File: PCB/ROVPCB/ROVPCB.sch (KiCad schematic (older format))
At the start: 7 parts, among them J1 Conn_01x04_Male, J2 Conn_01x04_Male, P1 Conn_02x20_Odd_Even

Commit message: Added Accelerometer to schematic and Board.
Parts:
- added C1: 10nF, Capacitor_SMD:C_0603_1608Metric, symbol Device:C
- added C2: 0.1uF, Capacitor_SMD:C_0603_1608Metric, symbol Device:C
- added C3: 2.2 nF, Capacitor_SMD:C_0603_1608Metric, symbol Device:C
- added U1: MPU-6050, Sensor_Motion:InvenSense_QFN-24_4x4mm_P0.5mm, symbol Sensor_Motion:MPU-6050
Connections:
- wire segments 63 -> 81
- no-connect marks 0 -> 3
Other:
- note added: "Accelerometer"
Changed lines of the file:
@@
 Wire Wire Line
 	7100 2250 8050 2250
+$Comp
+L Sensor_Motion:MPU-6050 U1
+U 1 1 5C61FB5F
+P 2550 5350
+F 0 "U1" H 2550 4564 50  0000 C CNN
+F 1 "MPU-6050" H 2550 4473 50  0000 C CNN
+F 2 "Sensor_Motion:InvenSense_QFN-24_4x4mm_P0.5mm" H 2550 4550 50  0001 C CNN
+F 3 "https://store.invensense.com/datasheets/invensense/MPU-6050_DataSheet_V3%204.pdf" H 2550 5200 50  0001 C CNN
+	1    2550 5350
+	1    0    0    -1
+$EndComp
+Text Notes 1650 4050 0    157  ~ 31
+Accelerometer
+$Comp
+L ROVPCB-rescue:GND-power #PWR0101
+U 1 1 5C61FCB6
+P 1700 5700
+F 0 "#PWR0101" H 1700 5450 50  0001 C CNN
+F 1 "GND" H 1700 5550 50  0000 C CNN
+F 2 "" H 1700 5700 50  0000 C CNN
+F 3 "" H 1700 5700 50  0000 C CNN
+	1    1700 5700
+	1    0    0    -1
+$EndComp
+Wire Wire Line
+	1850 5550 1700 5550
+Wire Wire Line
+	1700 5550 1700 5650
+Wire Wire Line
+	1850 5650 1800 5650
+Connection ~ 1700 5650
+Wire Wire Line
+	1700 5650 1700 5700
+$Comp
+L Device:C C2
+U 1 1 5C622699
+P 3450 5800
+F 0 "C2" H 3565 5846 50  0000 L CNN
+F 1 "0.1uF" H 3565 5755 50  0000 L CNN
+F 2 "Capacitor_SMD:C_0603_1608Metric" H 3488 5650 50  0001 C CNN
+F 3 "~" H 3450 5800 50  0001 C CNN
+	1    3450 5800
+	1    0    0    -1
+$EndComp
+$Comp
+L Device:C C3
+U 1 1 5C622707
+P 3900 5800
+F 0 "C3" H 4015 5846 50  0000 L CNN
+F 1 "2.2 nF" H 4015 5755 50  0000 L CNN
+F 2 "Capacitor_SMD:C_0603_1608Metric" H 3938 5650 50  0001 C CNN
+F 3 "~" H 3900 5800 50  0001 C CNN
+	1    3900 5800
+	1    0    0    -1
+$EndComp
+Wire Wire Line
+	3250 5650 3450 5650
+$Comp
+L ROVPCB-rescue:GND-power #PWR0102
+U 1 1 5C62556F
+P 3450 5950
+F 0 "#PWR0102" H 3450 5700 50  0001 C CNN
+F 1 "GND" H 3450 5800 50  0000 C CNN
+F 2 "" H 3450 5950 50  0000 C CNN
+F 3 "" H 3450 5950 50  0000 C CNN
+	1    3450 5950
+	1    0    0    -1
+$EndComp
+$Comp
+L ROVPCB-rescue:GND-power #PWR0103
+U 1 1 5C62558E
+P 3900 5950
+F 0 "#PWR0103" H 3900 5700 50  0001 C CNN
+F 1 "GND" H 3900 5800 50  0000 C CNN
+F 2 "" H 3900 5950 50  0000 C CNN
+F 3 "" H 3900 5950 50  0000 C CNN
+	1    3900 5950
+	1    0    0    -1
+$EndComp
+Wire Wire Line
+	3900 5550 3900 5650
+Wire Wire Line
+	3250 5550 3900 5550
+$Comp
+L Device:C C1
+U 1 1 5C626E58
+P 2000 4450
+F 0 "C1" H 2115 4496 50  0000 L CNN
+F 1 "10nF" H 2115 4405 50  0000 L CNN
+F 2 "Capacitor_SMD:C_0603_1608Metric" H 2038 4300 50  0001 C CNN
+F 3 "~" H 2000 4450 50  0001 C CNN
+	1    2000 4450
+	1    0    0    -1
+$EndComp
+$Comp
+L ROVPCB-rescue:GND-power #PWR0104
+U 1 1 5C626ED8
+P 2000 4600
+F 0 "#PWR0104" H 2000 4350 50  0001 C CNN
+F 1 "GND" H 2000 4450 50  0000 C CNN
+F 2 "" H 2000 4600 50  0000 C CNN
+F 3 "" H 2000 4600 50  0000 C CNN
+	1    2000 4600
+	1    0    0    -1
+$EndComp
+Wire Wire Line
+	2450 4650 2450 4200
+Wire Wire Line
+	2450 4200 2000 4200
+Wire Wire Line
+	2000 4200 2000 4300
+Wire Wire Line
+	1850 5250 1700 5250
+Wire Wire Line
+	1700 5250 1700 5550
+Connection ~ 1700 5550
+$Comp
+L ROVPCB-rescue:+3.3V-power #PWR0105
+U 1 1 5C62A4AF
+P 2650 4400
+F 0 "#PWR0105" H 2650 4250 50  0001 C CNN
+F 1 "+3.3V" H 2650 4540 50  0000 C CNN
+F 2 "" H 2650 4400 50  0000 C CNN
+F 3 "" H 2650 4400 50  0000 C CNN
+	1    2650 4400
+	1    0    0    -1
+$EndComp
+Wire Wire Line
+	2650 4650 2650 4400
+NoConn ~ 3250 5250
+NoConn ~ 3250 5050
+NoConn ~ 3250 5350
+Text Label 1300 5050 0    50   ~ 0
+GPIO2(SDA1)
+Text Label 1300 5150 0    50   ~ 0
+GPIO3(SCL1)
+Wire Wire Line
+	1300 5150 1850 5150
+Wire Wire Line
+	1850 5050 1300 5050
+Wire Wire Line
+	2550 6050 1800 6050
+Wire Wire Line
+	1800 6050 1800 5650
+Connection ~ 1800 5650
+Wire Wire Line
+	1800 5650 1700 5650
 $EndSCHEMATC

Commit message: Filling in Display cutout on PCB
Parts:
- MK1, MK2, MK3, MK4: symbol ROVPCB-rescue:Mounting_Hole-Mechanical -> ROVPCB-rescue:Mounting_Hole-Mechanical-ROVPCB-rescue
- P1: symbol ROVPCB-rescue:Conn_02x20_Odd_Even-Connector_Generic -> ROVPCB-rescue:Conn_02x20_Odd_Even-Connector_Generic-ROVPCB-rescue
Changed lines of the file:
@@
 $EndDescr
 $Comp
-L ROVPCB-rescue:+5V-power #PWR01
+L ROVPCB-rescue:+5V-power-ROVPCB-rescue #PWR01
 U 1 1 580C1B61
 P 3100 950
@@
 Connection ~ 3100 1100
 $Comp
-L ROVPCB-rescue:GND-power #PWR02
+L ROVPCB-rescue:GND-power-ROVPCB-rescue #PWR02
 U 1 1 580C1D11
 P 3000 3150
@@
 Connection ~ 3000 2000
 $Comp
-L ROVPCB-rescue:GND-power #PWR03
+L ROVPCB-rescue:GND-power-ROVPCB-rescue #PWR03
 U 1 1 580C1E01
 P 2300 3150
@@
 	2200 950  2200 1100
 $Comp
-L ROVPCB-rescue:+3.3V-power #PWR04
+L ROVPCB-rescue:+3.3V-power-ROVPCB-rescue #PWR04
 U 1 1 580C1BC1
 P 2200 950
@@
 ID_SD and ID_SC PINS:\nThese pins are reserved for HAT ID EEPROM.\n\nAt boot time this I2C interface will be\ninterrogated to look for an EEPROM\nthat identifes the attached board and\nallows automagic setup of the GPIOs\n(and optionally, Linux drivers).\n\nDO NOT USE these pins for anything other\nthan attaching an I2C ID EEPROM. Leave\nunconnected if ID EEPROM not required.
 $Comp
-L ROVPCB-rescue:Mounting_Hole-Mechanical MK1
+L ROVPCB-rescue:Mounting_Hole-Mechanical-ROVPCB-rescue MK1
 U 1 1 5834FB2E
 P 3000 7200
@@
 $EndComp
 $Comp
-L ROVPCB-rescue:Mounting_Hole-Mechanical MK3
+L ROVPCB-rescue:Mounting_Hole-Mechanical-ROVPCB-rescue MK3
 U 1 1 5834FBEF
 P 3450 7200
@@
 $EndComp
 $Comp
-L ROVPCB-rescue:Mounting_Hole-Mechanical MK2
+L ROVPCB-rescue:Mounting_Hole-Mechanical-ROVPCB-rescue MK2
 U 1 1 5834FC19
 P 3000 7400
@@
 $EndComp
 $Comp
-L ROVPCB-rescue:Mounting_Hole-Mechanical MK4
+L ROVPCB-rescue:Mounting_Hole-Mechanical-ROVPCB-rescue MK4
 U 1 1 5834FC4F
 P 3450 7400
@@
 Mounting Holes
 $Comp
-L ROVPCB-rescue:Conn_02x20_Odd_Even-Connector_Generic P1
+L ROVPCB-rescue:Conn_02x20_Odd_Even-Connector_Generic-ROVPCB-rescue P1
 U 1 1 59AD464A
 P 2600 2000
@@
 GPIO3(SCL1)
 $Comp
-L ROVPCB-rescue:GND-power #PWR06
+L ROVPCB-rescue:GND-power-ROVPCB-rescue #PWR06
 U 1 1 5C61D5CB
 P 8400 2350
@@
 $EndComp
 $Comp
-L ROVPCB-rescue:+3.3V-power #PWR05
+L ROVPCB-rescue:+3.3V-power-ROVPCB-rescue #PWR05
 U 1 1 5C61D5E4
 P 8150 1450
@@
 Accelerometer
 $Comp
-L ROVPCB-rescue:GND-power #PWR0101
+L ROVPCB-rescue:GND-power-ROVPCB-rescue #PWR0101
 U 1 1 5C61FCB6
 P 1700 5700
@@
 	3250 5650 3450 5650
 $Comp
-L ROVPCB-rescue:GND-power #PWR0102
+L ROVPCB-rescue:GND-power-ROVPCB-rescue #PWR0102
 U 1 1 5C62556F
 P 3450 5950
@@
 $EndComp
 $Comp
-L ROVPCB-rescue:GND-power #PWR0103
+L ROVPCB-rescue:GND-power-ROVPCB-rescue #PWR0103
 U 1 1 5C62558E
 P 3900 5950
@@
 $EndComp
 $Comp
-L ROVPCB-rescue:GND-power #PWR0104
+L ROVPCB-rescue:GND-power-ROVPCB-rescue #PWR0104
 U 1 1 5C626ED8
 P 2000 4600
@@
 Connection ~ 1700 5550
 $Comp
-L ROVPCB-rescue:+3.3V-power #PWR0105
+L ROVPCB-rescue:+3.3V-power-ROVPCB-rescue #PWR0105
 U 1 1 5C62A4AF
 P 2650 4400

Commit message: New accelerometer and added the Humdity/Temp/Pressure Sensor
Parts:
- removed U1: MPU-6050, Sensor_Motion:InvenSense_QFN-24_4x4mm_P0.5mm, symbol Sensor_Motion:MPU-6050
- added U1: MPU-9250, Sensor_Motion:InvenSense_QFN-24_3x3mm_P0.4mm, symbol Sensor_Motion:MPU-9250
- added U2: BME280, Package_LGA:Bosch_LGA-8_2.5x2.5mm_P0.65mm_ClockwisePinNumbering, symbol Sensor:BME280
- C1: value 10nF -> 0.1uF
- C3: value 2.2 nF -> 0.1uF
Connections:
- wire segments 81 -> 98
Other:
- note added: "Lux"
- note added: "Temp/Press/Humid"
- moved on the sheet: C2

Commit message: Added all the things
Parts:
- added R1: 10k, Resistor_SMD:R_0805_2012Metric, symbol Device:R
- added U3: LIGHT_TSL2591, Adafruit TSL2591:DFN6_TAOS, symbol Adafruit_TSL2591-eagle-import:LIGHT_TSL2591
- added U?: LTC4316IDDPBF, LTC4316IDDPBF:DFN-10_DD, symbol LTC4316IDDPBF:LTC4316IDDPBF
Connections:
- net +3V3: now also R1.2, U3.5 (VDD); no longer U1.9 (AD0/MISO)
- net GND: now also U3.3 (GND)
- net GPIO2(SDA1): now also U3.6 (SDA)
- net GPIO3(SCL1): now also U3.1 (SCL)
- new net: R1.1, U1.9 (AD0/MISO)
- no-connect marks 3 -> 31
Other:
- note added: "I2C Address Translator"
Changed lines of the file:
@@
 $EndComp
 Wire Wire Line
-	3100 950  3100 1100
+	3100 950  3100 1000
 Wire Wire Line
 	3100 1100 2900 1100
@@
 L ROVPCB-rescue:+3.3V-power-ROVPCB-rescue #PWR0104
 U 1 1 5CB71953
-P 1050 5000
-F 0 "#PWR0104" H 1050 4850 50  0001 C CNN
-F 1 "+3.3V" H 1050 5140 50  0000 C CNN
-F 2 "" H 1050 5000 50  0000 C CNN
-F 3 "" H 1050 5000 50  0000 C CNN
-	1    1050 5000
-	1    0    0    -1
-$EndComp
-Wire Wire Line
-	1750 5100 1050 5100
-Wire Wire Line
-	1050 5100 1050 5000
+P 1000 4800
+F 0 "#PWR0104" H 1000 4650 50  0001 C CNN
+F 1 "+3.3V" H 1000 4940 50  0000 C CNN
+F 2 "" H 1000 4800 50  0000 C CNN
+F 3 "" H 1000 4800 50  0000 C CNN
+	1    1000 4800
+	1    0    0    -1
+$EndComp
 $Comp
 L ROVPCB-rescue:GND-power-ROVPCB-rescue #PWR0106
@@
 Connection ~ 5200 5900
 Wire Wire Line
-	5200 5900 5200 6100
+	5200 5900 5200 6000
 $Comp
 L ROVPCB-rescue:GND-power-ROVPCB-rescue #PWR0111
@@
 Text Notes 4200 3750 0    138  ~ 28
 Lux
+$Comp
+L Adafruit_TSL2591-eagle-import:LIGHT_TSL2591 U3
+U 1 1 5CB6F38A
+P 5350 4300
+F 0 "U3" H 5577 4290 42  0000 L CNN
+F 1 "LIGHT_TSL2591" H 5577 4211 42  0000 L CNN
+F 2 "Adafruit TSL2591:DFN6_TAOS" H 5350 4300 50  0001 C CNN
+F 3 "" H 5350 4300 50  0001 C CNN
+	1    5350 4300
+	1    0    0    -1
+$EndComp
+$Comp
+L ROVPCB-rescue:+3.3V-power-ROVPCB-rescue #PWR07
+U 1 1 5CB72608
+P 4600 4500
+F 0 "#PWR07" H 4600 4350 50  0001 C CNN
+F 1 "+3.3V" H 4600 4640 50  0000 C CNN
+F 2 "" H 4600 4500 50  0000 C CNN
+F 3 "" H 4600 4500 50  0000 C CNN
+	1    4600 4500
+	1    0    0    -1
+$EndComp
+Wire Wire Line
+	4600 4500 4950 4500
+$Comp
+L ROVPCB-rescue:GND-power-ROVPCB-rescue #PWR08
+U 1 1 5CB7546E
+P 4800 4600
+F 0 "#PWR08" H 4800 4350 50  0001 C CNN
+F 1 "GND" H 4800 4450 50  0000 C CNN
+F 2 "" H 4800 4600 50  0000 C CNN
+F 3 "" H 4800 4600 50  0000 C CNN
+	1    4800 4600
+	1    0    0    -1
+$EndComp
+Wire Wire Line
+	4950 4600 4800 4600
+Text Label 4450 4100 0    50   ~ 0
+GPIO2(SDA1)
+Wire Wire Line
+	4950 4100 4450 4100
+Text Label 4450 4200 0    50   ~ 0
+GPIO3(SCL1)
+Wire Wire Line
+	4450 4200 4950 4200
+NoConn ~ 4950 4300
+NoConn ~ 4950 4400
+NoConn ~ 3950 1400
+NoConn ~ 3950 1500
+NoConn ~ 3950 1600
+NoConn ~ 3950 1800
+NoConn ~ 3950 1900
+NoConn ~ 3950 2100
+NoConn ~ 3950 2200
+NoConn ~ 3950 2300
+NoConn ~ 3950 2400
+NoConn ~ 3950 2600
+NoConn ~ 3950 2800
+NoConn ~ 3950 2900
+NoConn ~ 3950 3000
+NoConn ~ 1250 2900
+NoConn ~ 1250 2800
+NoConn ~ 1250 2700
+NoConn ~ 1250 2600
+NoConn ~ 1250 2500
+NoConn ~ 1250 2400
+NoConn ~ 1250 2200
+NoConn ~ 1250 2100
+NoConn ~ 1250 2000
+NoConn ~ 1250 1800
+NoConn ~ 1250 1700
+NoConn ~ 1250 1600
+NoConn ~ 1250 1400
+$Comp
+L power:PWR_FLAG #FLG0101
+U 1 1 5CBD550D
+P 5200 6000
+F 0 "#FLG0101" H 5200 6075 50  0001 C CNN
+F 1 "PWR_FLAG" V 5200 6128 50  0000 L CNN
+F 2 "" H 5200 6000 50  0001 C CNN
+F 3 "~" H 5200 6000 50  0001 C CNN
+	1    5200 6000
+	0    1    1    0
+$EndComp
+Connection ~ 5200 6000
+Wire Wire Line
+	5200 6000 5200 6100
+$Comp
+L power:PWR_FLAG #FLG0102
+U 1 1 5CBD5948
+P 3100 1000
+F 0 "#FLG0102" H 3100 1075 50  0001 C CNN
+F 1 "PWR_FLAG" V 3100 1128 50  0000 L CNN
+F 2 "" H 3100 1000 50  0001 C CNN
+F 3 "~" H 3100 1000 50  0001 C CNN
+	1    3100 1000
+	0    1    1    0
+$EndComp
+Connection ~ 3100 1000
+Wire Wire Line
+	3100 1000 3100 1100
+$Comp
+L Device:R R1
+U 1 1 5CBD8F78
+P 1000 4950
+F 0 "R1" H 930 4904 50  0000 R CNN
+F 1 "10k" H 930 4995 50  0000 R CNN
+F 2 "Resistor_SMD:R_0805_2012Metric" V 930 4950 50  0001 C CNN
+F 3 "~" H 1000 4950 50  0001 C CNN
+	1    1000 4950
+	-1   0    0    1
+$EndComp
+Wire Wire Line
+	1000 5100 1750 5100
+Text Notes 7750 4750 0    138  ~ 28
+I2C Address Translator
+$Comp
+L LTC4316IDDPBF:LTC4316IDDPBF U?
+U 1 1 5CBEE417
+P 7200 5300
+F 0 "U?" H 8825 5665 50  0000 C CNN
+F 1 "LTC4316IDDPBF" H 8825 5574 50  0000 C CNN
+F 2 "LTC4316IDDPBF:DFN-10_DD" H 10750 4800 50  0001 L BNN
+F 3 "LTC4316IDD#PBF-ND" H 10550 5300 50  0001 L BNN
+F 4 "Linear Technology/Analog" H 10400 5600 50  0001 L BNN "Field4"
+F 5 "LTC4316 - Single I2C/SMBus Address Translator" H 10000 5450 50  0001 L BNN "Field5"
+F 6 "LTC4316IDD#PBF" H 10650 4950 50  0001 L BNN "Field7"
+F 7 "DFN-10 Linear Technology" H 10450 5150 50  0001 L BNN "Field8"
+	1    7200 5300
+	1    0    0    -1
+$EndComp
 $EndSCHEMATC

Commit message: HouseKeepinggit add *
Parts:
- MK1, MK2, MK3, MK4: symbol ROVPCB-rescue:Mounting_Hole-Mechanical-ROVPCB-rescue -> ROVPCB-rescue:Mounting_Hole-Mechanical-ROVPCB-rescue-ROVPCB-rescue
- P1: symbol ROVPCB-rescue:Conn_02x20_Odd_Even-Connector_Generic-ROVPCB-rescue -> ROVPCB-rescue:Conn_02x20_Odd_Even-Connector_Generic-ROVPCB-rescue-ROVPCB-rescue
- gave numbers to parts that had none: 1
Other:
- note added: "Atlas Scientific board"
- moved on the sheet: C3, J1, J2, U2, U3, U4

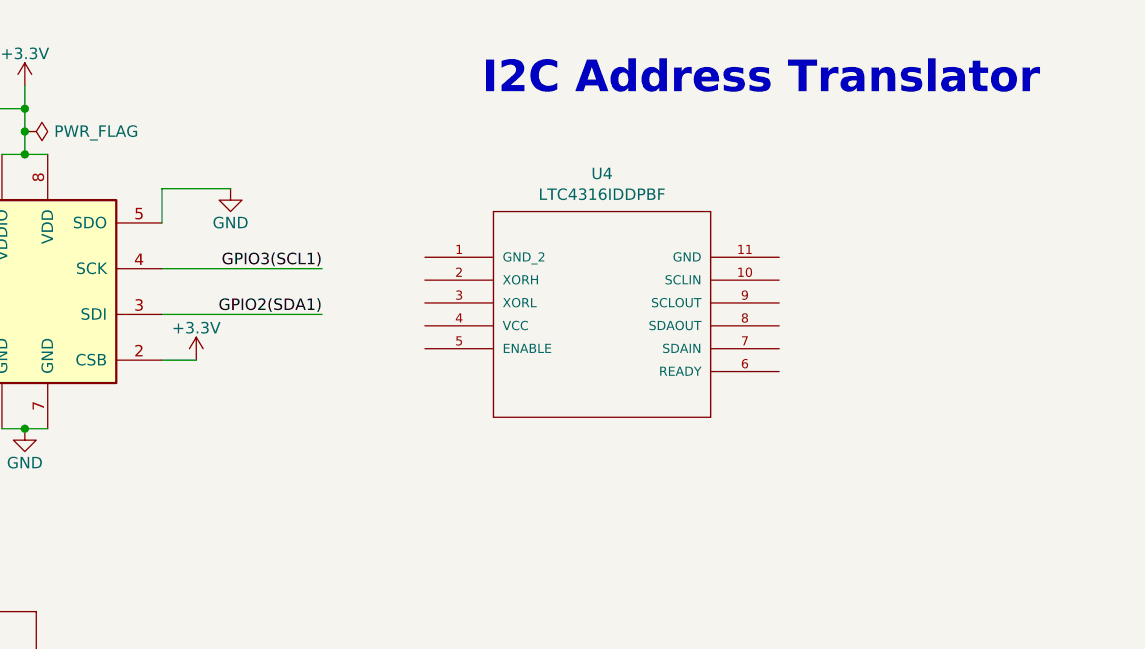
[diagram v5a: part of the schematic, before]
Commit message: Added I2C Address Translator
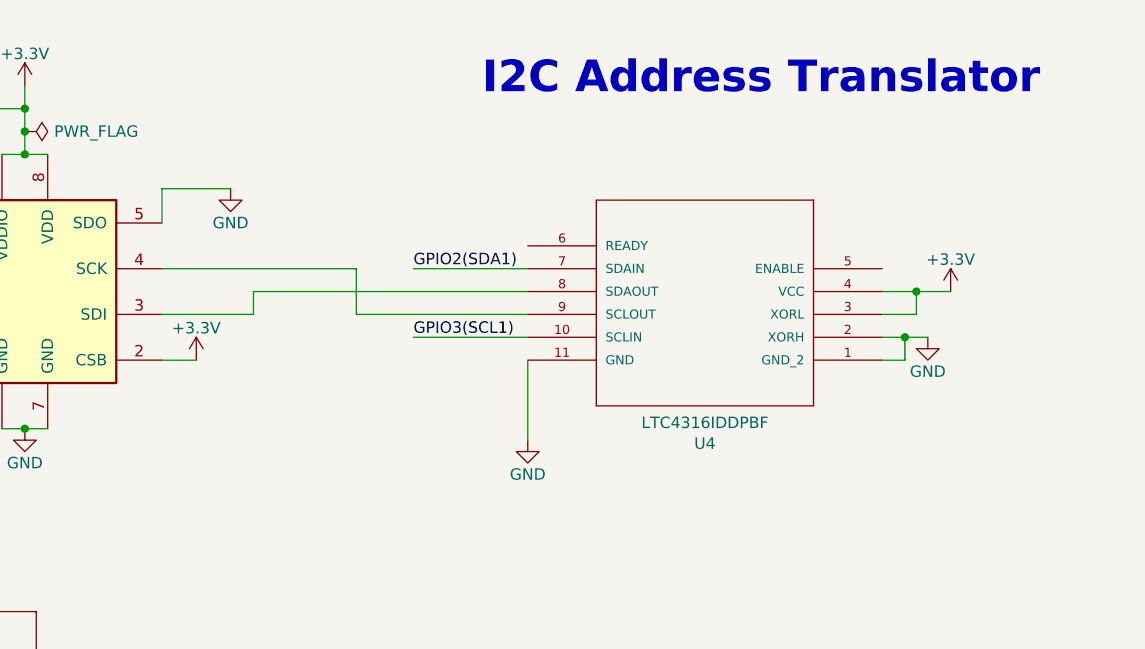
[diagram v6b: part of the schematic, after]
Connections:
- net +3V3: now also U4.3 (XORL), U4.4 (VCC)
- net GND: now also U4.1 (GND_2), U4.11 (GND), U4.2 (XORH)
- net GPIO2(SDA1): now also U4.7 (SDAIN); no longer U2.3 (SDI)
- net GPIO3(SCL1): now also U4.10 (SCLIN); no longer U2.4 (SCK)
- net at U4.8 (SDAOUT): now also U2.3 (SDI)
- net at U4.9 (SCLOUT): now also U2.4 (SCK)
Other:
- moved on the sheet: U4
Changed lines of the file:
@@
 $EndComp
-Wire Wire Line
-	6600 5250 5900 5250
-Wire Wire Line
-	6600 5450 5900 5450
 Wire Wire Line
 	6200 4900 5900 4900
 Wire Wire Line
 	5900 4900 5900 5050
-Text Label 6600 5450 2    50   ~ 0
-GPIO2(SDA1)
-Text Label 6600 5250 2    50   ~ 0
-GPIO3(SCL1)
 Text Notes 4000 6500 0    138  ~ 28
 Lux
@@
 L LTC4316IDDPBF:LTC4316IDDPBF U4
 U 1 1 5CBEE417
-P 6200 5200
-F 0 "U4" H 7825 5565 50  0000 C CNN
-F 1 "LTC4316IDDPBF" H 7825 5474 50  0000 C CNN
-F 2 "LTC4316IDDPBF:DFN-10_DD" H 9750 4700 50  0001 L BNN
-F 3 "LTC4316IDD#PBF-ND" H 9550 5200 50  0001 L BNN
-F 4 "Linear Technology/Analog" H 9400 5500 50  0001 L BNN "Field4"
-F 5 "LTC4316 - Single I2C/SMBus Address Translator" H 9000 5350 50  0001 L BNN "Field5"
-F 6 "LTC4316IDD#PBF" H 9650 4850 50  0001 L BNN "Field7"
-F 7 "DFN-10 Linear Technology" H 9450 5050 50  0001 L BNN "Field8"
-	1    6200 5200
-	1    0    0    -1
+P 9900 5650
+F 0 "U4" H 11525 6015 50  0000 C CNN
+F 1 "LTC4316IDDPBF" H 11525 5924 50  0000 C CNN
+F 2 "LTC4316IDDPBF:DFN-10_DD" H 13450 5150 50  0001 L BNN
+F 3 "LTC4316IDD#PBF-ND" H 13250 5650 50  0001 L BNN
+F 4 "Linear Technology/Analog" H 13100 5950 50  0001 L BNN "Field4"
+F 5 "LTC4316 - Single I2C/SMBus Address Translator" H 12700 5800 50  0001 L BNN "Field5"
+F 6 "LTC4316IDD#PBF" H 13350 5300 50  0001 L BNN "Field7"
+F 7 "DFN-10 Linear Technology" H 13150 5500 50  0001 L BNN "Field8"
+	1    9900 5650
+	-1   0    0    1
 $EndComp
 Text Notes 7600 1000 0    138  ~ 28
 Atlas Scientific board
+Text Label 7000 5250 0    50   ~ 0
+GPIO2(SDA1)
+Text Label 7000 5550 0    50   ~ 0
+GPIO3(SCL1)
+Wire Wire Line
+	7000 5550 7500 5550
+Wire Wire Line
+	7000 5250 7500 5250
+$Comp
+L ROVPCB-rescue:GND-power-ROVPCB-rescue-ROVPCB-rescue #PWR?
+U 1 1 5CB8FA80
+P 7500 6000
+F 0 "#PWR?" H 7500 5750 50  0001 C CNN
+F 1 "GND" H 7500 5850 50  0000 C CNN
+F 2 "" H 7500 6000 50  0000 C CNN
+F 3 "" H 7500 6000 50  0000 C CNN
+	1    7500 6000
+	1    0    0    -1
+$EndComp
+Wire Wire Line
+	7500 5650 7500 6000
+Wire Wire Line
+	7500 5350 6300 5350
+Wire Wire Line
+	6300 5350 6300 5450
+Wire Wire Line
+	6300 5450 5900 5450
+Wire Wire Line
+	5900 5250 6750 5250
+Wire Wire Line
+	6750 5250 6750 5450
+Wire Wire Line
+	6750 5450 7500 5450
+$Comp
+L ROVPCB-rescue:GND-power-ROVPCB-rescue-ROVPCB-rescue #PWR?
+U 1 1 5CBA3506
+P 9250 5550
+F 0 "#PWR?" H 9250 5300 50  0001 C CNN
+F 1 "GND" H 9250 5400 50  0000 C CNN
+F 2 "" H 9250 5550 50  0000 C CNN
+F 3 "" H 9250 5550 50  0000 C CNN
+	1    9250 5550
+	1    0    0    -1
+$EndComp
+Wire Wire Line
+	9250 5550 9150 5550
+$Comp
+L ROVPCB-rescue:+3.3V-power-ROVPCB-rescue-ROVPCB-rescue #PWR?
+U 1 1 5CBA6BEC
+P 9350 5350
+F 0 "#PWR?" H 9350 5200 50  0001 C CNN
+F 1 "+3.3V" H 9350 5490 50  0000 C CNN
+F 2 "" H 9350 5350 50  0000 C CNN
+F 3 "" H 9350 5350 50  0000 C CNN
+	1    9350 5350
+	1    0    0    -1
+$EndComp
+Wire Wire Line
+	9350 5350 9200 5350
+Wire Wire Line
+	9200 5350 9200 5450
+Wire Wire Line
+	9200 5450 9050 5450
+Connection ~ 9200 5350
+Wire Wire Line
+	9200 5350 9050 5350
+Wire Wire Line
+	9050 5650 9150 5650
+Wire Wire Line
+	9150 5650 9150 5550
+Connection ~ 9150 5550
+Wire Wire Line
+	9150 5550 9050 5550
 $EndSCHEMATC
